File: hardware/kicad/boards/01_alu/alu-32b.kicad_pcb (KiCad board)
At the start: 4 copper layers, 220 x 220 mm, 146 parts, among them J1 Conn_02x16_Odd_Even, J2 Conn_02x16_Odd_Even, J3 Conn_02x04_Odd_Even, J4 Conn_02x16_Odd_Even, J5 Conn_02x16_Counter_Clockwise, SW1 SW_DIP_x08, SW10 SW_DIP_x08, SW11 SW_DIP_x08, SW12 SW_DIP_x08, SW13 SW_DIP_x08, SW2 SW_DIP_x08, SW3 SW_DIP_x08, SW4 SW_DIP_x08, SW5 SW_DIP_x08, SW6 SW_DIP_x08, SW7 SW_SPDT, SW8 SW_DIP_x08, SW9 SW_DIP_x08, U17 74HC86, U19 74HC00, U20 74LS283, U21 74AC251, U22 74AC251, U23 74AC251, U24 74AC251, U27 74HC86, U29 74HC00, U30 74LS283, U31 74AC251, U32 74AC251, U33 74AC251, U34 74AC251, U37 74HC86, U39 74HC00, U40 74LS283, U41 74AC251, U42 74AC251, U43 74AC251, U44 74AC251, U47 74HC86, U49 74HC00, U50 74LS283, U51 74AC251, U52 74AC251, U53 74AC251, U54 74AC251, U57 74HC86, U59 74HC00, U60 74LS283, U61 74AC251, U62 74AC251, U63 74AC251, U64 74AC251, U67 74HC86, U69 74HC00, U70 74LS283, U71 74AC251, U72 74AC251, U73 74AC251, U74 74AC251, U77 74HC86, U79 74HC00, U80 74LS283, U81 74AC251, U82 74AC251, U83 74AC251, U84 74AC251, U87 74HC86, U89 74HC00, U90 74LS283, U91 74AC251, U92 74AC251, U93 74AC251, U94 74AC251

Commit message: pcb: routed 4b cell and propagated to x3 additional cells
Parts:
- removed U42, U43, U44, U51, U52, U53, U54, U61, U62, U63, U64, U71, U72, U73, U74, U81, U82, U83, U84, U91, U92, U93, U94: 74AC251, Package_SO:SOIC-16_3.9x9.9mm_P1.27mm
- added U1: 74ACT151, Package_SO:SOIC-16_3.9x9.9mm_P1.27mm, F.Cu at (111.0, 178.0)
- added U10: 74ACT151, Package_SO:SOIC-16_3.9x9.9mm_P1.27mm, F.Cu at (134.6, 245.0)
- added U11: 74ACT151, Package_SO:SOIC-16_3.9x9.9mm_P1.27mm, F.Cu at (123.1, 245.0)
- added U12: 74ACT151, Package_SO:SOIC-16_3.9x9.9mm_P1.27mm, F.Cu at (146.2, 245.0)
- added U13: 74ACT151, Package_SO:SOIC-16_3.9x9.9mm_P1.27mm, F.Cu at (111.2, 278.5)
- added U14: 74ACT151, Package_SO:SOIC-16_3.9x9.9mm_P1.27mm, F.Cu at (134.4, 278.5)
- added U15: 74ACT151, Package_SO:SOIC-16_3.9x9.9mm_P1.27mm, F.Cu at (122.9, 278.5)
- added U16: 74ACT151, Package_SO:SOIC-16_3.9x9.9mm_P1.27mm, F.Cu at (146.0, 278.5)
- added U18: 74ACT151, Package_SO:SOIC-16_3.9x9.9mm_P1.27mm, F.Cu at (237.6, 240.2)
- added U2: 74ACT151, Package_SO:SOIC-16_3.9x9.9mm_P1.27mm, F.Cu at (122.8, 178.0)
- added U25: 74ACT151, Package_SO:SOIC-16_3.9x9.9mm_P1.27mm, F.Cu at (256.8, 205.5)
- added U26: 74ACT151, Package_SO:SOIC-16_3.9x9.9mm_P1.27mm, F.Cu at (245.4, 205.5)
- added U28: 74ACT151, Package_SO:SOIC-16_3.9x9.9mm_P1.27mm, F.Cu at (268.4, 205.5)
- added U3: 74ACT151, Package_SO:SOIC-16_3.9x9.9mm_P1.27mm, F.Cu at (134.2, 178.0)
- added U35: 74ACT151, Package_SO:SOIC-16_3.9x9.9mm_P1.27mm, F.Cu at (241.5, 136.3)
- added U36: 74ACT151, Package_SO:SOIC-16_3.9x9.9mm_P1.27mm, F.Cu at (264.7, 136.3)
- added U38: 74ACT151, Package_SO:SOIC-16_3.9x9.9mm_P1.27mm, F.Cu at (253.3, 136.3)
- added U4: 74ACT151, Package_SO:SOIC-16_3.9x9.9mm_P1.27mm, F.Cu at (145.8, 178.0)
- added U5: 74ACT151, Package_SO:SOIC-16_3.9x9.9mm_P1.27mm, F.Cu at (111.4, 211.5)
- added U6: 74ACT151, Package_SO:SOIC-16_3.9x9.9mm_P1.27mm, F.Cu at (134.6, 211.5)
- added U7: 74ACT151, Package_SO:SOIC-16_3.9x9.9mm_P1.27mm, F.Cu at (123.1, 211.5)
- added U8: 74ACT151, Package_SO:SOIC-16_3.9x9.9mm_P1.27mm, F.Cu at (146.2, 211.5)
- added U9: 74ACT151, Package_SO:SOIC-16_3.9x9.9mm_P1.27mm, F.Cu at (111.4, 245.0)
- U21, U22, U23, U24, U31, U32, U33, U34, U41: value 74AC251 -> 74ACT151
- moved U49 170.1 mm to (113.2, 290.5), turned to 90 degrees
- moved U50 164.5 mm to (142.9, 290.3), turned to 90 degrees
- moved U47 163.1 mm to (127.7, 290.4), turned to 90 degrees
- moved C58 162.6 mm to (107.1, 288.0), turned to 0 degrees
- moved C70 162.2 mm to (106.6, 273.1), turned to -90 degrees
- moved C64 162.2 mm to (141.4, 273.1), turned to -90 degrees
- moved C66 162.2 mm to (129.9, 273.1), turned to -90 degrees
- moved C68 162.2 mm to (118.4, 273.1), turned to -90 degrees
- moved C60 161.8 mm to (122.4, 288.5), turned to 90 degrees
- moved C62 160.6 mm to (136.9, 288.5), turned to 90 degrees
- moved C76 152.3 mm to (271.2, 254.2), turned to 180 degrees
- moved C120 145.5 mm to (270.9, 130.6), turned to 0 degrees
- moved C74 144.5 mm to (260.5, 254.2), turned to 180 degrees
- moved C72 139.5 mm to (249.0, 254.2), turned to 180 degrees
- moved U59 138.3 mm to (266.3, 248.8), turned to -90 degrees
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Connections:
- U21 pad 10: B0 -> B18
- U21 pad 11: A0 -> A18
- U21 pad 5: /alu-4b-0/log0 -> /alu-4b-4/log2
- U21 pad 9: C0 -> C18
- U22 pad 10: B1 -> B17
- U22 pad 11: A1 -> A17
- U22 pad 5: /alu-4b-0/log1 -> /alu-4b-4/log1
- U22 pad 9: C1 -> C17
- U23 pad 10: B2 -> B19
- U23 pad 11: A2 -> A19
- U23 pad 5: /alu-4b-0/log2 -> /alu-4b-4/log3
- U23 pad 9: C2 -> C19
- U24 pad 10: B3 -> B20
- U24 pad 11: A3 -> A20
- U24 pad 5: /alu-4b-0/log3 -> /alu-4b-5/log0
- U24 pad 9: C3 -> C20
- U31 pad 10: B4 -> B24
- U31 pad 11: A4 -> A24
- U31 pad 5: /alu-4b-1/log0 -> /alu-4b-6/log0
- U31 pad 9: C4 -> C24
- U32 pad 10: B6 -> B26
- U32 pad 11: A6 -> A26
- U32 pad 5: /alu-4b-1/log2 -> /alu-4b-6/log2
- U32 pad 9: C6 -> C26
- U33 pad 10: B5 -> B25
- U33 pad 11: A5 -> A25
- U33 pad 5: /alu-4b-1/log1 -> /alu-4b-6/log1
- U33 pad 9: C5 -> C25
- U34 pad 10: B7 -> B27
- U34 pad 11: A7 -> A27
- U34 pad 5: /alu-4b-1/log3 -> /alu-4b-6/log3
- U34 pad 9: C7 -> C27
- U41 pad 10: B8 -> B31
- U41 pad 11: A8 -> A31
- U41 pad 5: /alu-4b-2/log0 -> AEFF31
- U41 pad 9: C8 -> C31
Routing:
- net (no net): track 6864.0 -> 0.00 mm
- net B19: track 212.1 -> 0.00 mm
- net A19: track 211.7 -> 0.00 mm
- net C18: track 211.3 -> 0.00 mm
- net B18: track 210.9 -> 0.00 mm
- net A18: track 210.5 -> 0.00 mm
- net C17: track 210.1 -> 0.00 mm
- net B17: track 209.7 -> 0.00 mm
- net A17: track 208.6 -> 0.00 mm
- net C16: track 208.4 -> 0.00 mm
- net C31: track 208.0 -> 0.00 mm
- net C29: track 208.0 -> 0.00 mm
- net C28: track 208.0 -> 0.00 mm
- net C27: track 208.0 -> 0.00 mm
- net C26: track 208.0 -> 0.00 mm
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- added copper zone on B.Cu, net GND
- added copper zone on F.Cu, net VCC
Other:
- board size 220 x 220 mm -> 240 x 240 mm

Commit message: schematics: routed all 16b of board; laid out buses
Changed the clearance from 0.5mm to 0.25mm since ALU is purely combinational and max speed and edge goals remain large enough that crosstalk is extremely negligible at min mhz and 5v logic
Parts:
- U20, U30, U40, U50, U60, U70, U80, U90: value 74LS283 -> 74ACT283
- moved J5 238.1 mm to (158.5, 117.5), turned to 90 degrees
- moved U23 169.8 mm to (120.0, 315.0)
- moved U60 154.6 mm to (121.7, 326.7), turned to 90 degrees
- moved U59 151.0 mm to (136.9, 326.7), turned to 90 degrees
- moved C72 151.0 mm to (115.5, 324.8), turned to 90 degrees
- moved U21 149.1 mm to (131.8, 315.0)
- moved C74 147.0 mm to (131.5, 324.8), turned to 90 degrees
- moved C76 143.7 mm to (146.0, 324.8), turned to 90 degrees
- moved C80 138.5 mm to (139.5, 310.2), turned to 180 degrees
- moved C84 138.5 mm to (116.3, 310.2), turned to 180 degrees
- moved C78 138.4 mm to (151.2, 310.2), turned to 180 degrees
- moved C82 138.3 mm to (128.3, 310.2), turned to 180 degrees
- moved U22 129.9 mm to (143.2, 315.0)
- moved U57 121.2 mm to (151.4, 326.7), turned to 90 degrees
- moved U18 111.6 mm to (154.8, 315.0)
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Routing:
- net B0: track 17.2 -> 279.2 mm, vias 0 -> 2
- net B1: track 35.3 -> 251.0 mm, vias 1 -> 2
- net C0: track 13.6 -> 208.2 mm
- net A0: track 10.1 -> 201.3 mm
- net B4: track 17.2 -> 201.7 mm, vias 0 -> 2
- net ALU-OPCODE0: track 172.7 -> 350.0 mm, vias 16 -> 20
- net binv: track 186.6 -> 358.3 mm
- net C1: track 27.2 -> 191.7 mm
- net B8: track 17.2 -> 178.8 mm, vias 0 -> 2
- net A1: track 23.4 -> 185.0 mm
- net ALU-OPCODE1: track 180.5 -> 334.0 mm, vias 16 -> 20
- net B2: track 54.1 -> 200.4 mm, vias 1 -> 2
- net bsel: track 96.7 -> 238.3 mm, vias 8 -> 12
- net B12: track 17.2 -> 157.9 mm, vias 0 -> 2
- net B5: track 35.3 -> 174.0 mm, vias 1 -> 2
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- added copper zone on In1.Cu, net GND
- added copper zone on In2.Cu, net VCC
- removed copper zone on B.Cu, net GND
- removed copper zone on F.Cu, net VCC

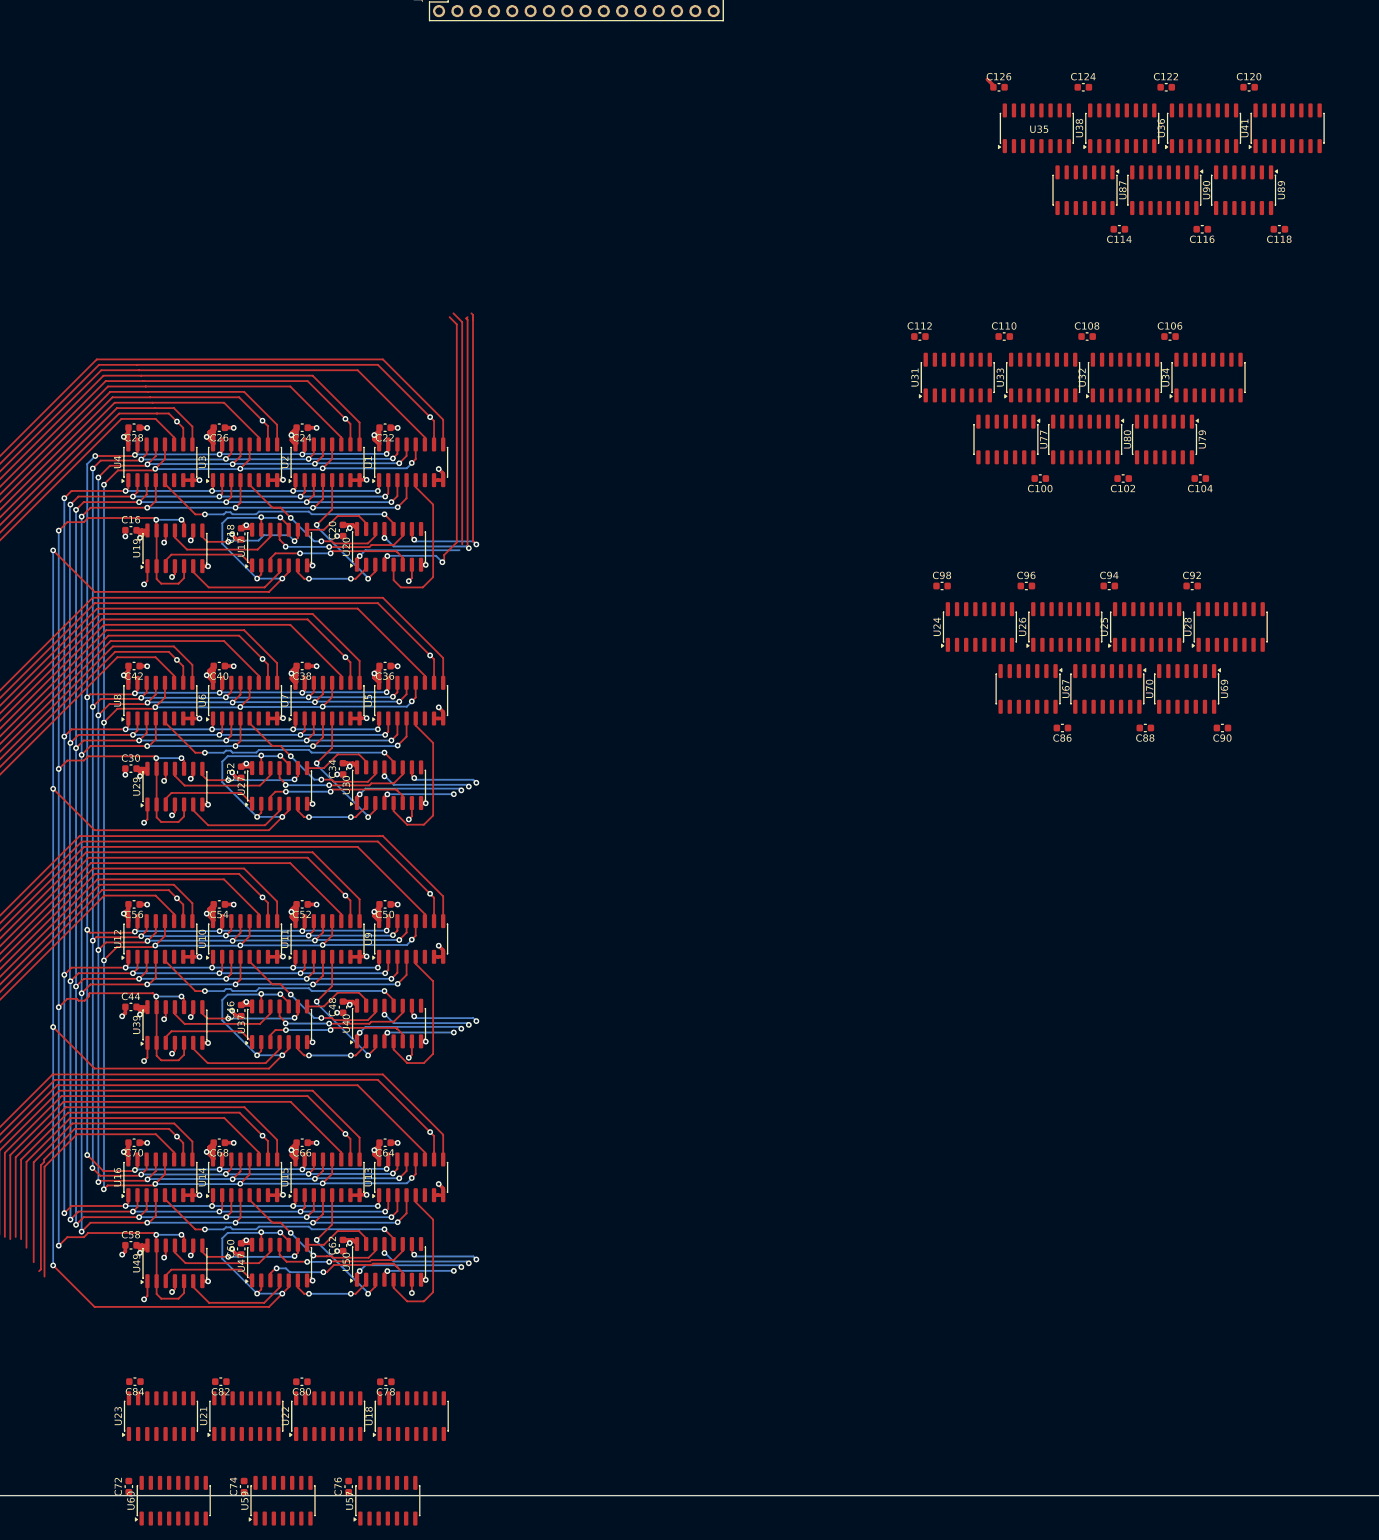
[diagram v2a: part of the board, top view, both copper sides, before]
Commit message: feat: routed all 32b; pending layout and final placements, interconnects, and DRC checks
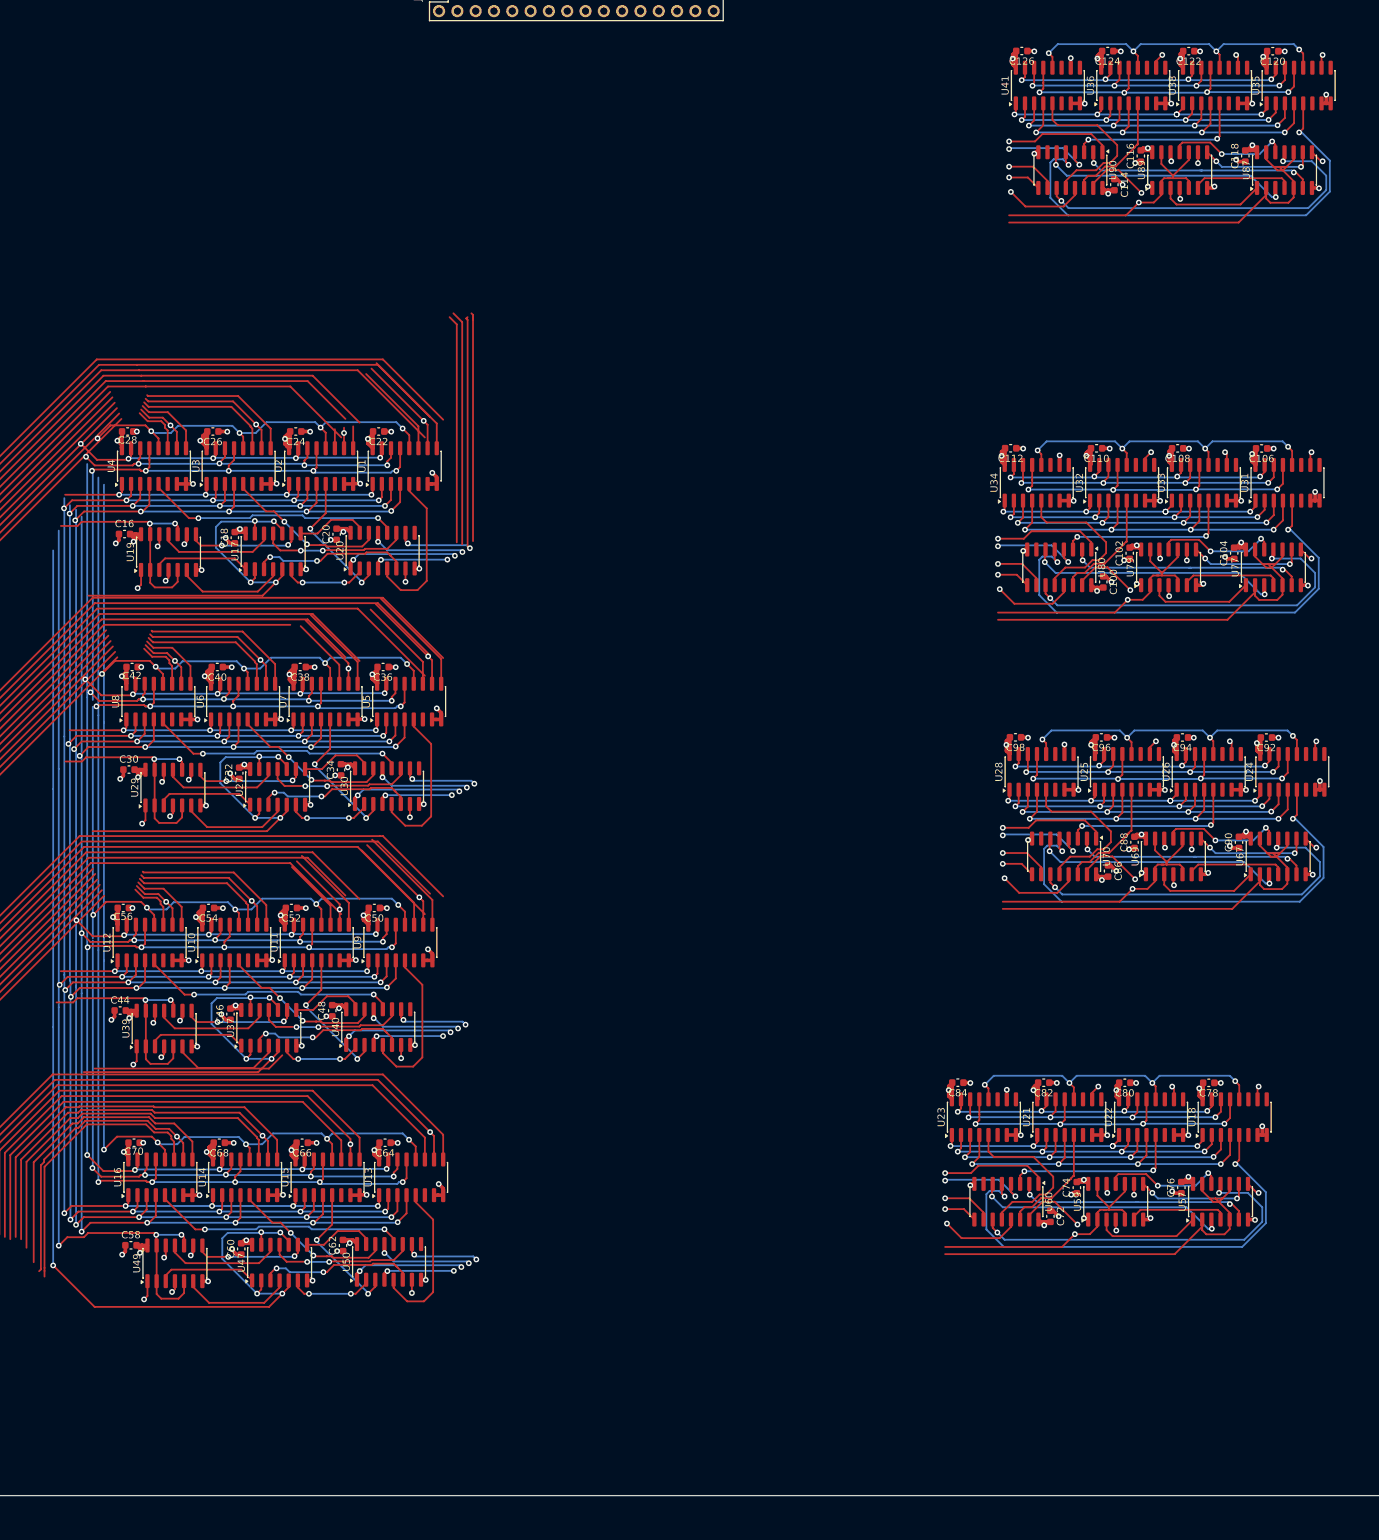
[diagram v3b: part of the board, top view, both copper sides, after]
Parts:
- moved C72 133.2 mm to (243.4, 287.2), turned to -90 degrees
- moved C74 122.7 mm to (247.0, 283.3)
- moved C76 122.7 mm to (261.5, 283.3)
- moved U60 122.7 mm to (237.3, 285.2), turned to -90 degrees
- moved U57 122.7 mm to (267.0, 285.2)
- moved U59 122.7 mm to (252.4, 285.2)
- moved C78 121.5 mm to (265.3, 268.7)
- moved C80 121.5 mm to (253.7, 268.7)
- moved C82 121.5 mm to (242.4, 268.7)
- moved U18 121.5 mm to (268.9, 273.5)
- moved U21 121.5 mm to (246.0, 273.5)
- moved U22 121.5 mm to (257.3, 273.5)
- moved U23 121.5 mm to (234.1, 273.5)
- moved C84 121.5 mm to (230.5, 268.7)
- moved U31 48.0 mm to (276.3, 185.5)
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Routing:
- net binv: track 358.3 -> 592.3 mm, vias 20 -> 17
- net C0: track 208.2 -> 421.5 mm
- net ALU-OPCODE0: track 350.0 -> 559.7 mm, vias 20 -> 36
- net ALU-OPCODE6: track 320.1 -> 522.7 mm, vias 20 -> 36
- net ALU-OPCODE1: track 334.0 -> 527.0 mm, vias 20 -> 36
- net B0: track 279.2 -> 88.4 mm
- net ALU-OPCODE5: track 304.0 -> 490.0 mm, vias 20 -> 36
- net C1: track 191.7 -> 377.1 mm
- net B1: track 251.0 -> 66.5 mm
- net ALU-OPCODE2: track 320.5 -> 498.4 mm, vias 20 -> 36
- net ALU-OPCODE7: track 332.6 -> 510.4 mm, vias 20 -> 36
- net ALU-OPCODE4: track 289.5 -> 460.9 mm, vias 20 -> 36
- net ALU-OPCODE3: track 304.3 -> 465.4 mm, vias 20 -> 37
- net bsel: track 238.3 -> 385.7 mm, vias 12 -> 13
- net VCC: track 168.5 -> 304.5 mm, vias 28 -> 56
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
